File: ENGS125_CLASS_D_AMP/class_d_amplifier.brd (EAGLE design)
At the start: 100 x 80 mm, 19 parts, among them M1 ???, M2 ???, U1 LTC6992, U2 LTC4449

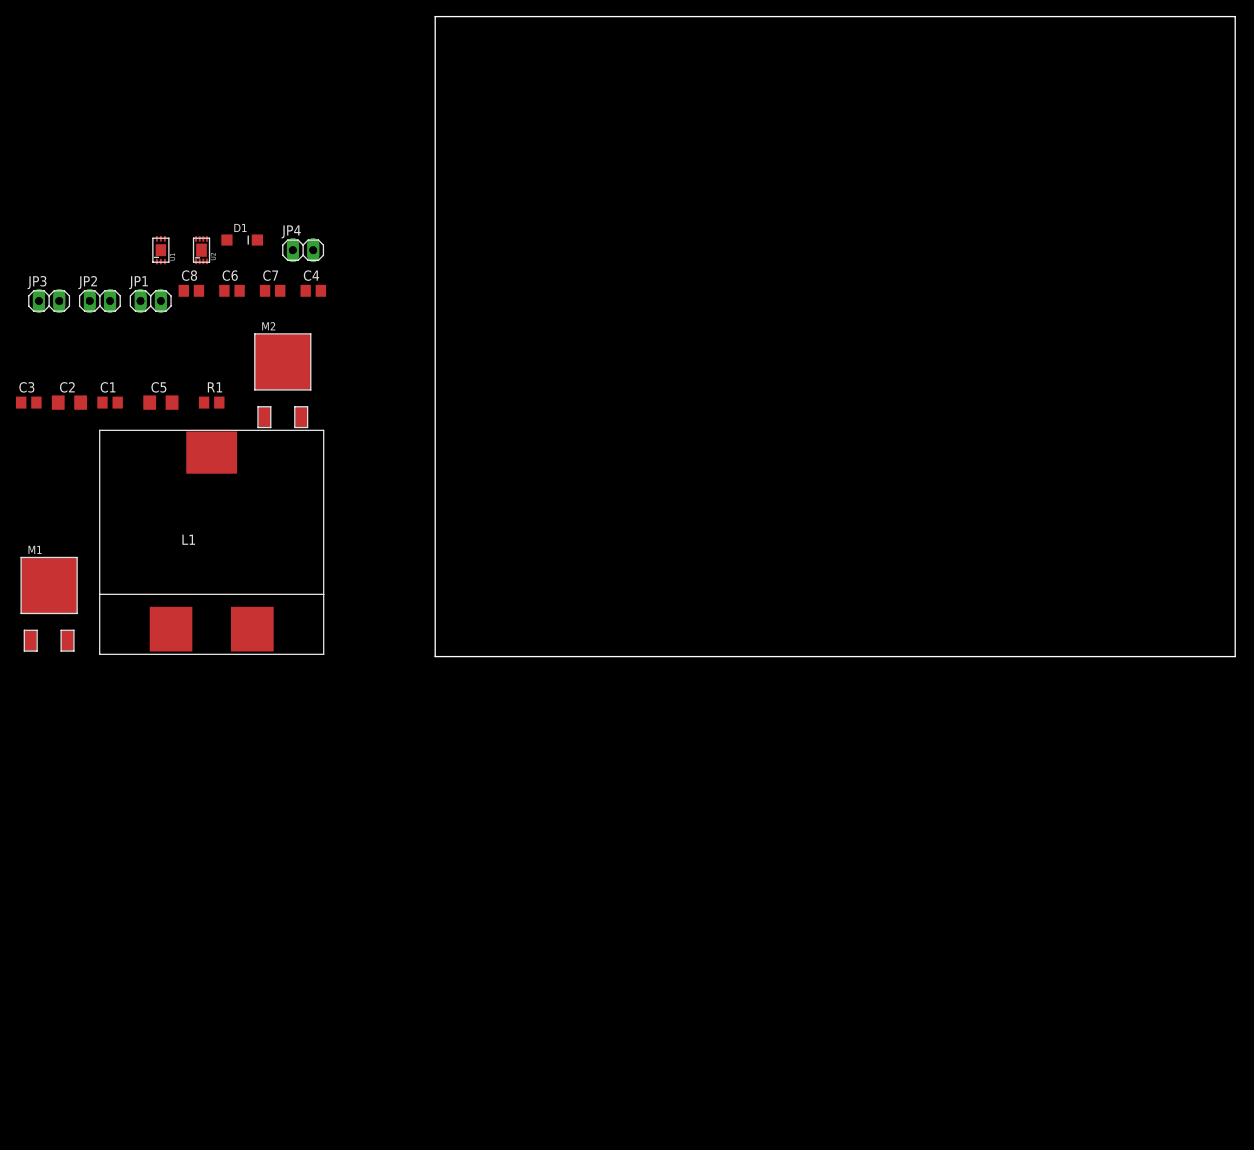
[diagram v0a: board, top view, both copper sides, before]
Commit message: Added banana jacks and edited schematic.
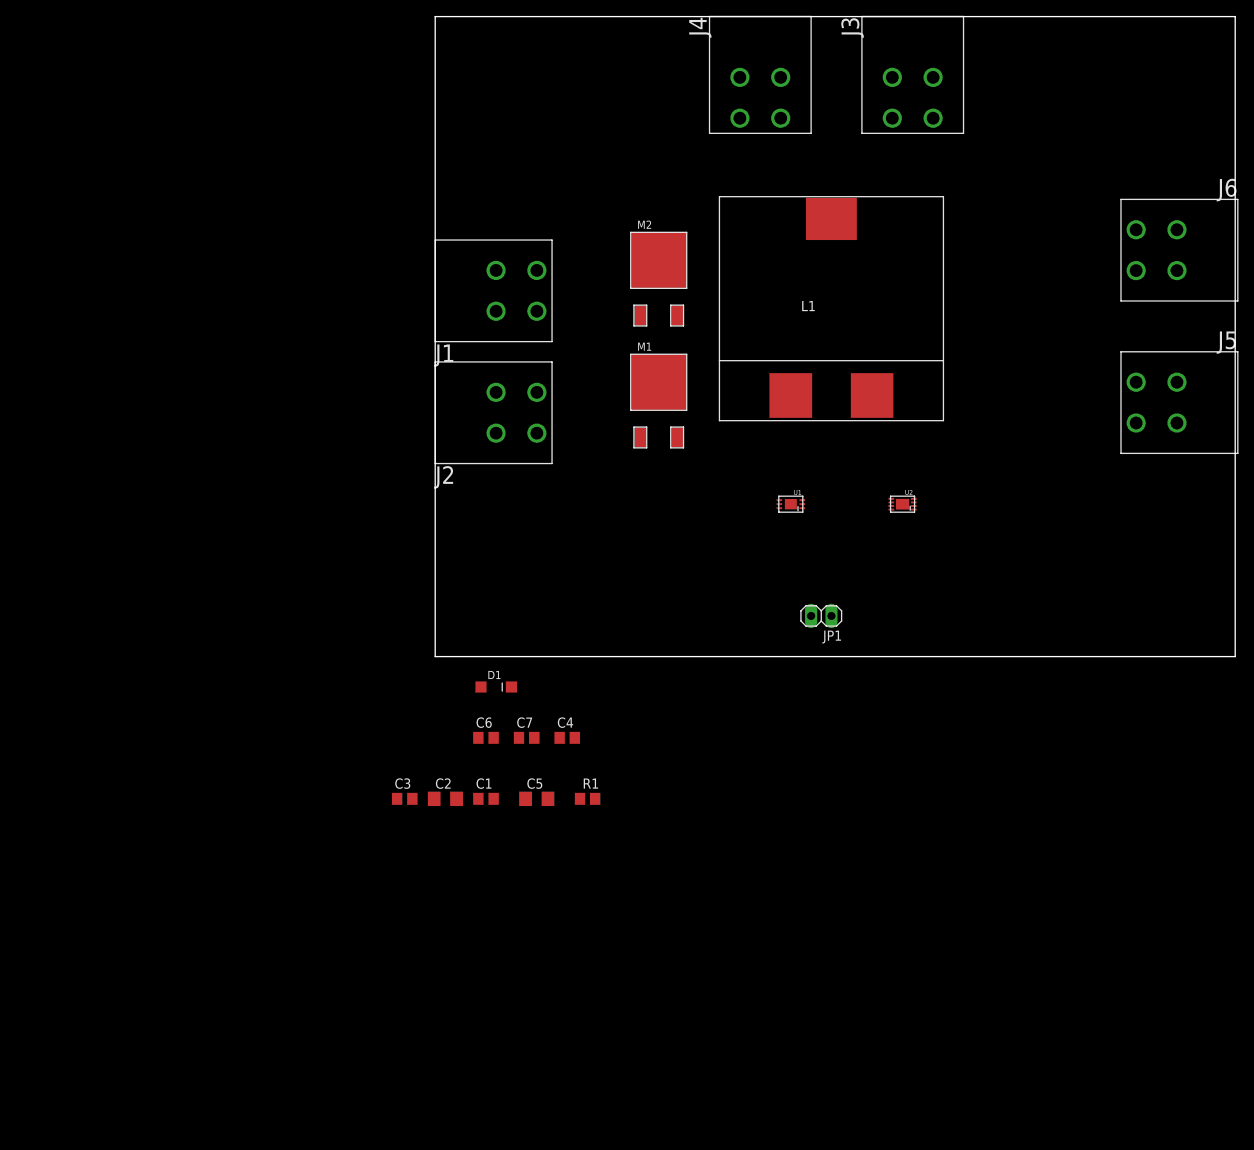
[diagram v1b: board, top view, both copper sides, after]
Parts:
- removed C8: ???, Engs125_library:C0805
- removed JP2, JP3, JP4: (no value), Engs125_library:1X02
- added J1, J2, J3, J4, J5, J6: BANANA_JACK_CT3151, Engs125_lib_UPDATEFeb22:CT3151SP2_PCB_MOUNT
- C2: value ??? -> 1.5u
- C6: value ??? -> 0.1u
- JP1: device Engs125_library:1X02 -> Engs125_lib_UPDATEFeb22:1X02
- L1: value ??? -> 33u
- M1, M2: value ??? -> AUIRLR024ZTRL
- moved U2 93.2 mm to (58.4, 19.1), turned to 90 degrees
- moved JP1 92.6 mm to (48.3, 5.08), turned to 180 degrees
- moved U1 84.9 mm to (44.5, 19.1), turned to 90 degrees
- moved L1 82.8 mm to (49.5, 47.0)
- moved M1 80.3 mm to (27.9, 34.3)
- moved C1 68.3 mm to (6.35, -17.8)
- moved C2 68.3 mm to (1.27, -17.8)
- moved R1 68.3 mm to (19.1, -17.8)
- moved C3 68.3 mm to (-3.81, -17.8)
- moved C5 68.3 mm to (12.7, -17.8)
- moved D1 64.3 mm to (7.62, -3.81)
- moved C4 64.3 mm to (16.5, -10.2)
- moved C6 64.3 mm to (6.35, -10.2)
- moved C7 64.3 mm to (11.4, -10.2)
- moved M2 48.7 mm to (27.9, 49.5)
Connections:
- removed net VAC: C8.2, JP4.1
- removed net VDC: C2.1, C6.1, C8.1, L1.2
- new net VOUT: C2.1, C6.1, J5.P$1, J5.P$2, J5.P$3, J5.P$4, L1.2
- net GND: now also J2.P$1, J2.P$2, J2.P$3, J2.P$4, J4.P$1, J4.P$2, J4.P$3, J4.P$4, J6.P$1, J6.P$2, J6.P$3, J6.P$4; no longer JP2.2, JP3.2, JP4.2
- net VGG: now also J1.P$1, J1.P$2, J1.P$3, J1.P$4; no longer JP2.1
- net VIN: now also J3.P$1, J3.P$2, J3.P$3, J3.P$4; no longer JP1.1
- net VREF: now also JP1.1; no longer JP3.1

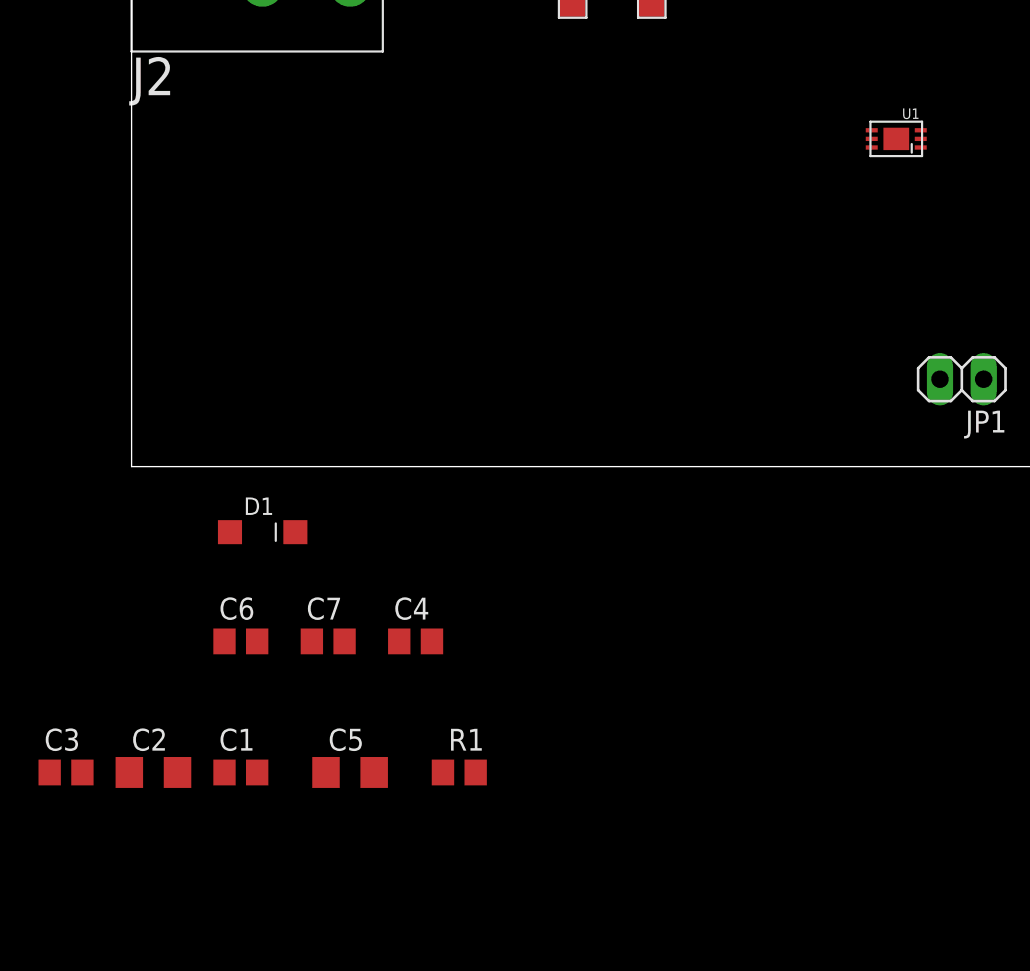
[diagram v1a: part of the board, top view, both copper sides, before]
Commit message: Updated package for LTC6992 (PWM modulator)
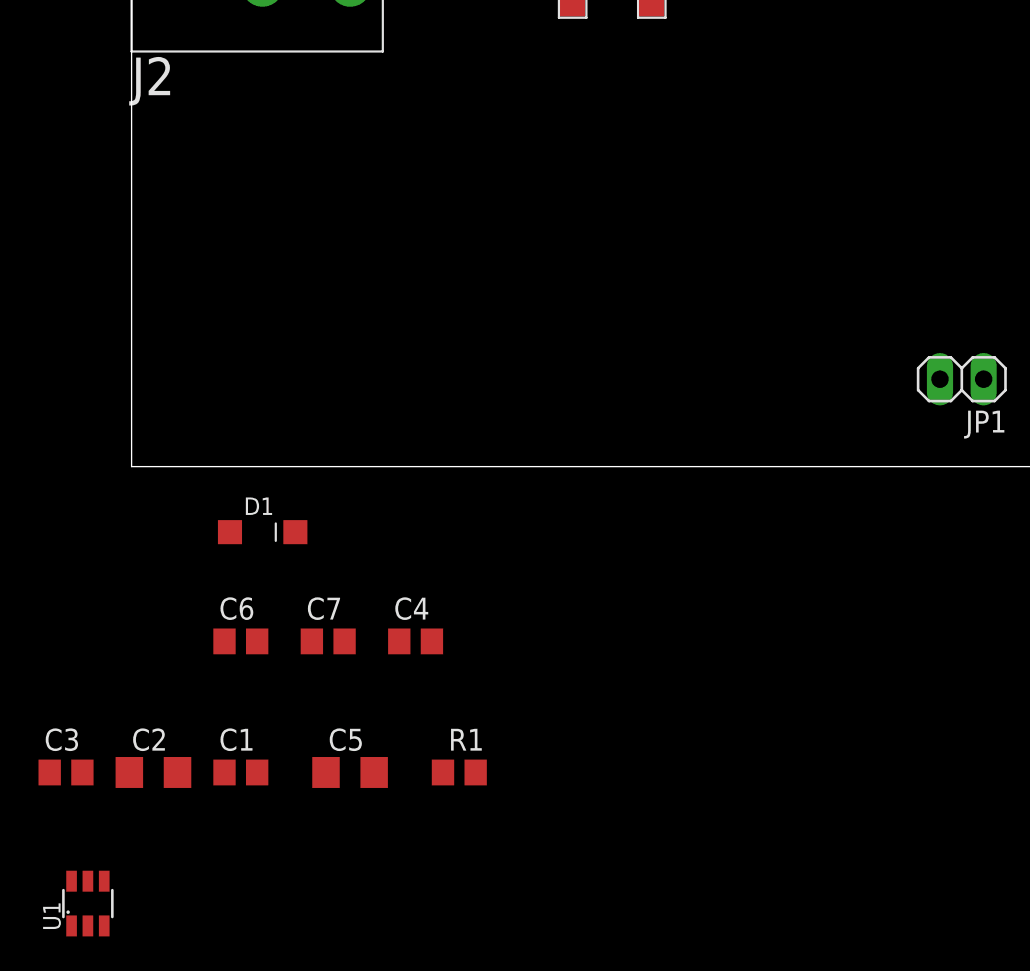
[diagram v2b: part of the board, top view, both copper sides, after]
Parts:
- U1: value LTC6992 -> LTC6992TSOT-23; device Engs125_library:LTC6992 -> Engs125_lib_UPDATEFeb22:TSOT23-6
- moved U1 64.7 mm to (-2.54, -25.4), turned to 0 degrees
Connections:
- new net N$3: U1.2
- net GND: now also U1.4; no longer U1.2, U1.5, U1.7
- net VGG: now also U1.5; no longer U1.1
- net VREF: now also U1.1; no longer U1.4
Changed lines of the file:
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@@
 <attribute name="VALUE" x="18.415" y="-20.32" size="1.27" layer="27"/>
-</element>
-<element name="U1" library="Engs125_library" package="LTC6992" value="LTC6992" x="44.45" y="19.05" smashed="yes" rot="R90">
-<attribute name="NAME" x="45.81" y="20.82" size="0.6096" layer="25" rot="R180"/>
-<attribute name="VALUE" x="45.81" y="17.85" size="0.6096" layer="27" rot="R180"/>
 </element>
 <element name="U2" library="Engs125_library" package="DCB8" value="LTC4449" x="58.42" y="19.05" smashed="yes" rot="R90">
@@
 <attribute name="NAME" x="100.33" y="59.69" size="2.1844" layer="25" font="vector" rot="R180"/>
 </element>
+<element name="U1" library="Engs125_lib_UPDATEFeb22" package="TSOT23-6" value="LTC6992TSOT-23" x="-2.54" y="-25.4" smashed="yes">
+<attribute name="NAME" x="-4.1275" y="-26.9875" size="1.016" layer="25" ratio="10" rot="R90"/>
+<attribute name="VALUE" x="0.3175" y="-26.9875" size="1.016" layer="27" ratio="10" rot="R90"/>
+</element>
 </elements>
 <signals>
 <signal name="N$1">
+<contactref element="R1" pad="2"/>
 <contactref element="U1" pad="3"/>
-<contactref element="R1" pad="2"/>
-<wire x1="20" y1="-17.78" x2="45.875" y2="19.55" width="0" layer="19" extent="1-1"/>
+<wire x1="20" y1="-17.78" x2="-1.59" y2="-26.7" width="0" layer="19" extent="1-1"/>
 </signal>
 <signal name="GND">
 <contactref element="R1" pad="1"/>
-<contactref element="U1" pad="2"/>
 <contactref element="C3" pad="2"/>
 <contactref element="C4" pad="2"/>
@@
 <contactref element="U2" pad="4"/>
 <contactref element="U2" pad="9"/>
-<contactref element="U1" pad="5"/>
-<contactref element="U1" pad="7"/>
 <contactref element="JP1" pad="2"/>
 <contactref element="J2" pad="P$4"/>
@@
 <contactref element="J6" pad="P$3"/>
 <contactref element="J6" pad="P$2"/>
+<contactref element="U1" pad="4"/>
+<wire x1="87.62" y1="53.35" x2="92.72" y2="53.35" width="0" layer="19" extent="1-1"/>
 <wire x1="92.72" y1="48.25" x2="92.72" y2="53.35" width="0" layer="19" extent="1-1"/>
-<wire x1="87.62" y1="53.35" x2="92.72" y2="53.35" width="0" layer="19" extent="1-1"/>
-<wire x1="87.62" y1="48.25" x2="92.72" y2="48.25" width="0" layer="19" extent="1-1"/>
-<wire x1="38.09" y1="72.4" x2="92.72" y2="48.25" width="0" layer="19" extent="1-1"/>
-<wire x1="43.19" y1="72.4" x2="38.09" y2="72.4" width="0" layer="19" extent="1-1"/>
-<wire x1="38.09" y1="67.3" x2="38.09" y2="72.4" width="0" layer="19" extent="1-1"/>
-<wire x1="43.19" y1="67.3" x2="43.19" y2="72.4" width="0" layer="19" extent="1-1"/>
-<wire x1="7.61" y1="27.93" x2="43.19" y2="72.4" width="0" layer="19" extent="1-1"/>
-<wire x1="12.71" y1="27.93" x2="7.61" y2="27.93" width="0" layer="19" extent="1-1"/>
-<wire x1="7.61" y1="33.03" x2="7.61" y2="27.93" width="0" layer="19" extent="1-1"/>
-<wire x1="12.71" y1="33.03" x2="12.71" y2="27.93" width="0" layer="19" extent="1-1"/>
-<wire x1="46.99" y1="5.08" x2="12.71" y2="27.93" width="0" layer="19" extent="1-1"/>
-<wire x1="-2.86" y1="-17.78" x2="12.71" y2="33.03" width="0" layer="19" extent="1-1"/>
-<wire x1="2.67" y1="-17.78" x2="-2.86" y2="-17.78" width="0" layer="19" extent="1-1"/>
-<wire x1="14.1" y1="-17.78" x2="2.67" y2="-17.78" width="0" layer="19" extent="1-1"/>
-<wire x1="18.1" y1="-17.78" x2="14.1" y2="-17.78" width="0" layer="19" extent="1-1"/>
-<wire x1="30.24" y1="42.63" x2="18.1" y2="-17.78" width="0" layer="19" extent="1-1"/>
-<wire x1="7.3" y1="-10.16" x2="18.1" y2="-17.78" width="0" layer="19" extent="1-1"/>
-<wire x1="12.38" y1="-10.16" x2="7.3" y2="-10.16" width="0" layer="19" extent="1-1"/>
-<wire x1="17.46" y1="-10.16" x2="12.38" y2="-10.16" width="0" layer="19" extent="1-1"/>
-<wire x1="59.82" y1="19.725" x2="7.3" y2="-10.16" width="0" layer="19" extent="1-1"/>
+<wire x1="87.62" y1="48.25" x2="87.62" y2="53.35" width="0" layer="19" extent="1-1"/>
+<wire x1="59.82" y1="19.725" x2="87.62" y2="48.25" width="0" layer="19" extent="1-1"/>
 <wire x1="58.42" y1="19.05" x2="59.82" y2="19.725" width="0" layer="19" extent="1-1"/>
-<wire x1="44.45" y1="19.05" x2="58.42" y2="19.05" width="0" layer="19" extent="1-1"/>
-<wire x1="43.025" y1="19.05" x2="44.45" y2="19.05" width="0" layer="19" extent="1-1"/>
-<wire x1="45.875" y1="19.05" x2="44.45" y2="19.05" width="0" layer="19" extent="1-1"/>
+<wire x1="46.99" y1="5.08" x2="58.42" y2="19.05" width="0" layer="19" extent="1-1"/>
+<wire x1="17.46" y1="-10.16" x2="46.99" y2="5.08" width="0" layer="19" extent="1-1"/>
+<wire x1="12.38" y1="-10.16" x2="17.46" y2="-10.16" width="0" layer="19" extent="1-1"/>
+<wire x1="7.3" y1="-10.16" x2="12.38" y2="-10.16" width="0" layer="19" extent="1-1"/>
+<wire x1="18.1" y1="-17.78" x2="17.46" y2="-10.16" width="0" layer="19" extent="1-1"/>
+<wire x1="14.1" y1="-17.78" x2="18.1" y2="-17.78" width="0" layer="19" extent="1-1"/>
+<wire x1="2.67" y1="-17.78" x2="7.3" y2="-10.16" width="0" layer="19" extent="1-1"/>
+<wire x1="-2.86" y1="-17.78" x2="2.67" y2="-17.78" width="0" layer="19" extent="1-1"/>
+<wire x1="-1.59" y1="-24.1" x2="-2.86" y2="-17.78" width="0" layer="19" extent="1-1"/>
+<wire x1="30.24" y1="42.63" x2="58.42" y2="19.05" width="0" layer="19" extent="1-1"/>
+<wire x1="12.71" y1="33.03" x2="30.24" y2="42.63" width="0" layer="19" extent="1-1"/>
+<wire x1="7.61" y1="33.03" x2="12.71" y2="33.03" width="0" layer="19" extent="1-1"/>
+<wire x1="12.71" y1="27.93" x2="12.71" y2="33.03" width="0" layer="19" extent="1-1"/>
+<wire x1="7.61" y1="27.93" x2="7.61" y2="33.03" width="0" layer="19" extent="1-1"/>
+<wire x1="38.09" y1="67.3" x2="30.24" y2="42.63" width="0" layer="19" extent="1-1"/>
+<wire x1="43.19" y1="67.3" x2="38.09" y2="67.3" width="0" layer="19" extent="1-1"/>
+<wire x1="43.19" y1="72.4" x2="43.19" y2="67.3" width="0" layer="19" extent="1-1"/>
+<wire x1="38.09" y1="72.4" x2="38.09" y2="67.3" width="0" layer="19" extent="1-1"/>
 </signal>
 <signal name="VGG">
-<contactref element="U1" pad="1"/>
 <contactref element="C3" pad="1"/>
 <contactref element="C4" pad="1"/>
@@
 <contactref element="J1" pad="P$3"/>
 <contactref element="J1" pad="P$2"/>
-<wire x1="7.61" y1="48.27" x2="7.61" y2="43.17" width="0" layer="19" extent="1-1"/>
-<wire x1="12.71" y1="43.17" x2="7.61" y2="43.17" width="0" layer="19" extent="1-1"/>
-<wire x1="12.71" y1="48.27" x2="7.61" y2="48.27" width="0" layer="19" extent="1-1"/>
-<wire x1="-4.76" y1="-17.78" x2="12.71" y2="48.27" width="0" layer="19" extent="1-1"/>
-<wire x1="45.875" y1="18.55" x2="-4.76" y2="-17.78" width="0" layer="19" extent="1-1"/>
-<wire x1="57.02" y1="18.825" x2="45.875" y2="18.55" width="0" layer="19" extent="1-1"/>
+<contactref element="U1" pad="5"/>
 <wire x1="57.02" y1="19.275" x2="57.02" y2="18.825" width="0" layer="19" extent="1-1"/>
-<wire x1="5.72" y1="-3.81" x2="57.02" y2="19.275" width="0" layer="19" extent="1-1"/>
+<wire x1="12.71" y1="43.17" x2="57.02" y2="19.275" width="0" layer="19" extent="1-1"/>
+<wire x1="12.71" y1="48.27" x2="12.71" y2="43.17" width="0" layer="19" extent="1-1"/>
+<wire x1="7.61" y1="48.27" x2="12.71" y2="48.27" width="0" layer="19" extent="1-1"/>
+<wire x1="7.61" y1="43.17" x2="12.71" y2="43.17" width="0" layer="19" extent="1-1"/>
+<wire x1="5.72" y1="-3.81" x2="7.61" y2="43.17" width="0" layer="19" extent="1-1"/>
 <wire x1="15.56" y1="-10.16" x2="5.72" y2="-3.81" width="0" layer="19" extent="1-1"/>
+<wire x1="-4.76" y1="-17.78" x2="5.72" y2="-3.81" width="0" layer="19" extent="1-1"/>
+<wire x1="-2.54" y1="-24.1" x2="-4.76" y2="-17.78" width="0" layer="19" extent="1-1"/>
 </signal>
 <signal name="VPWM">
+<contactref element="U2" pad="5"/>
 <contactref element="U1" pad="6"/>
-<contactref element="U2" pad="5"/>
-<wire x1="43.025" y1="18.55" x2="57.02" y2="19.725" width="0" layer="19" extent="1-1"/>
+<wire x1="-3.49" y1="-24.1" x2="57.02" y2="19.725" width="0" layer="19" extent="1-1"/>
 </signal>
 <signal name="N$2">
@@
 </signal>
 <signal name="VREF">
-<contactref element="U1" pad="4"/>
 <contactref element="JP1" pad="1"/>
-<wire x1="43.025" y1="19.55" x2="49.53" y2="5.08" width="0" layer="19" extent="1-1"/>
+<contactref element="U1" pad="1"/>
+<wire x1="-3.49" y1="-26.7" x2="49.53" y2="5.08" width="0" layer="19" extent="1-1"/>
+</signal>
+<signal name="N$3">
+<contactref element="U1" pad="2"/>
 </signal>
 </signals>
